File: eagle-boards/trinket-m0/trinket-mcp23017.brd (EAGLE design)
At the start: 60 x 41.6 mm, 8 parts, among them IC2 MCP23017SP, Q1 BC547

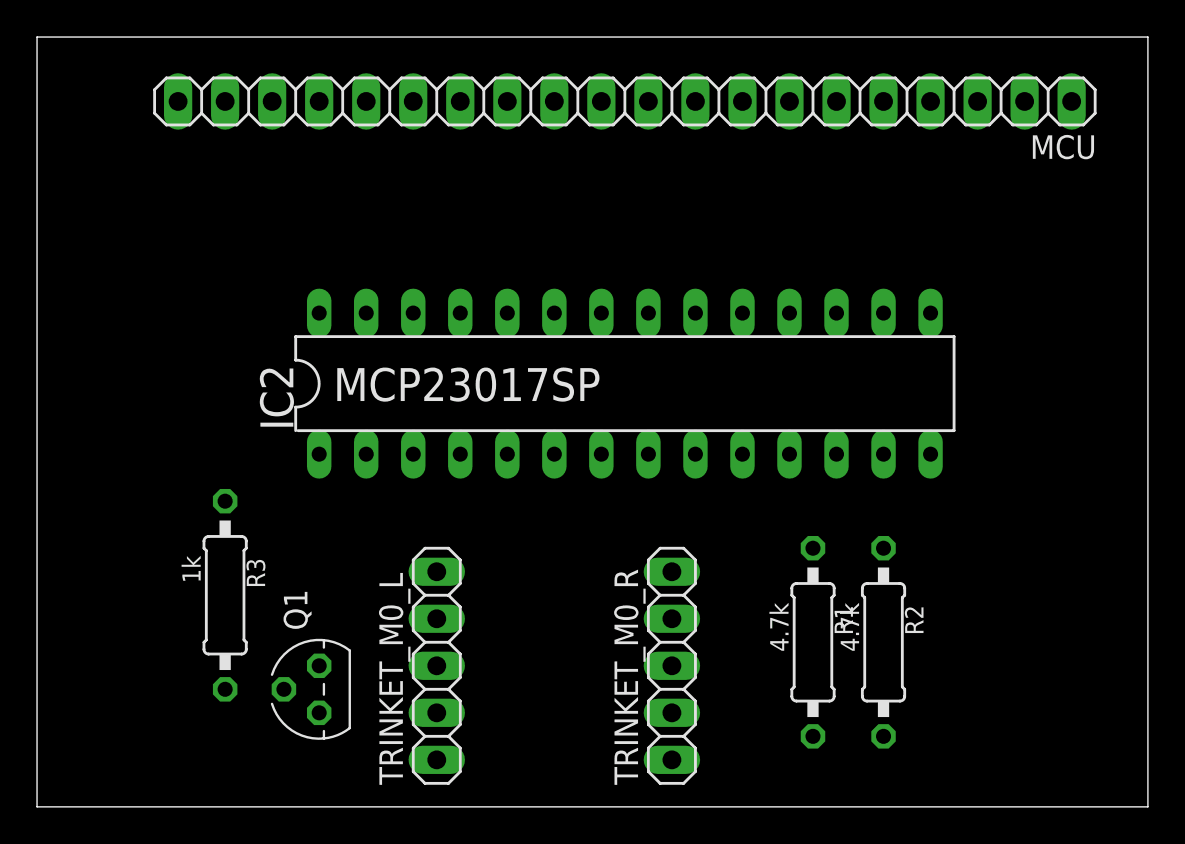
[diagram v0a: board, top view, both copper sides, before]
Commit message: Clean up the Trinket M0 based boards.
This makes the two board use the same size, and the same positioning of the common components.

It also reorients the silkscreen markings on the back to have the same orientation as the actuator board.

Also mark the used lines from the Trinket, as you can technically use any other MCU that can drive I²C.
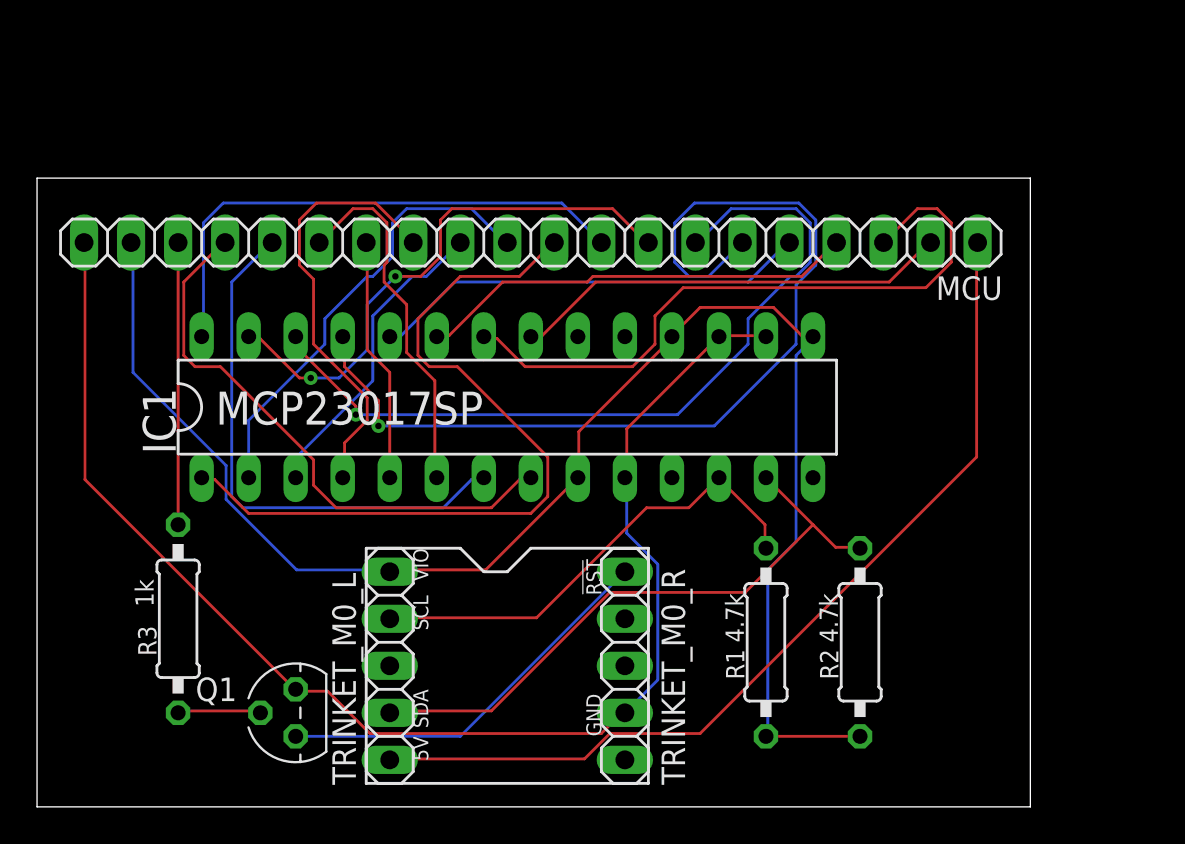
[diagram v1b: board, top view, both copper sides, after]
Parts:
- removed IC2: MCP23017SP, microchip:DIL28-3
- added IC1: MCP23017SP, microchip:DIL28-3
- moved MCU 9.16 mm to (26.7, 30.5)
- moved R3 2.84 mm to (7.62, 10.2)
- moved R1 2.54 mm to (39.4, 8.89)
- moved TRINKET_M0_L 2.54 mm to (19.1, 7.62)
- moved TRINKET_M0_R 2.54 mm to (31.8, 7.62)
- moved Q1 1.80 mm to (14.0, 5.08)
- moved R2 1.27 mm to (44.5, 8.89)
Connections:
- net +3V3: now also IC1.15, IC1.18, IC1.9; no longer IC2.15, IC2.18, IC2.9
- net GND: now also IC1.10, IC1.16, IC1.17; no longer IC2.10, IC2.16, IC2.17
- net N$1: now also IC1.21; no longer IC2.21
- net N$10: now also IC1.2; no longer IC2.2
- net N$11: now also IC1.3; no longer IC2.3
- net N$12: now also IC1.4; no longer IC2.4
- net N$13: now also IC1.5; no longer IC2.5
- net N$14: now also IC1.6; no longer IC2.6
- net N$15: now also IC1.7; no longer IC2.7
- net N$16: now also IC1.8; no longer IC2.8
- net N$2: now also IC1.22; no longer IC2.22
- net N$3: now also IC1.23; no longer IC2.23
- net N$4: now also IC1.24; no longer IC2.24
- net N$5: now also IC1.25; no longer IC2.25
- net N$6: now also IC1.26; no longer IC2.26
- net N$7: now also IC1.27; no longer IC2.27
- net N$8: now also IC1.28; no longer IC2.28
- net N$9: now also IC1.1; no longer IC2.1
- net SCL: now also IC1.12; no longer IC2.12
- net SDA: now also IC1.13; no longer IC2.13
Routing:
- net +3V3: track 0.00 -> 85.4 mm
- net GND: track 0.00 -> 74.8 mm
- net N$5: track 0.00 -> 52.5 mm, vias 0 -> 1
- net +5V: track 0.00 -> 50.1 mm
- net N$6: track 0.00 -> 43.7 mm, vias 0 -> 1
- net N$9: track 0.00 -> 42.3 mm
- net N$2: track 0.00 -> 36.0 mm
- net SDA: track 0.00 -> 33.8 mm
- net N$16: track 0.00 -> 30.8 mm
- net N$7: track 0.00 -> 29.7 mm, vias 0 -> 2
- net N$15: track 0.00 -> 29.2 mm
- net N$8: track 0.00 -> 29.0 mm
- net SCL: track 0.00 -> 25.8 mm
- net N$10: track 0.00 -> 24.4 mm
- net N$4: track 0.00 -> 23.7 mm
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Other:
- board size 60 x 41.6 mm -> 53.6 x 34 mm
- board text added: "!RST"
- board text added: "5V"
- board text added: "Birch Books Smart Home Controller Module Trinket M0 MCP23017 rev. 1b"
- board text added: "GND"
- board text added: "SCL"
- board text added: "SDA"
- board text added: "VIO"
- board text removed: "Birch Books Smart Home Controller Module Trinket M0 MCP23017 rev. 1a"
